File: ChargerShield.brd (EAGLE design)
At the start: 123.2 x 53.3 mm, 42 parts, among them IC1 LM324N, Q1 BD648, Q2 BC140-10, Q3 BC548, T2 BC548, X1 +5V, X2 Battery, X3 VCC

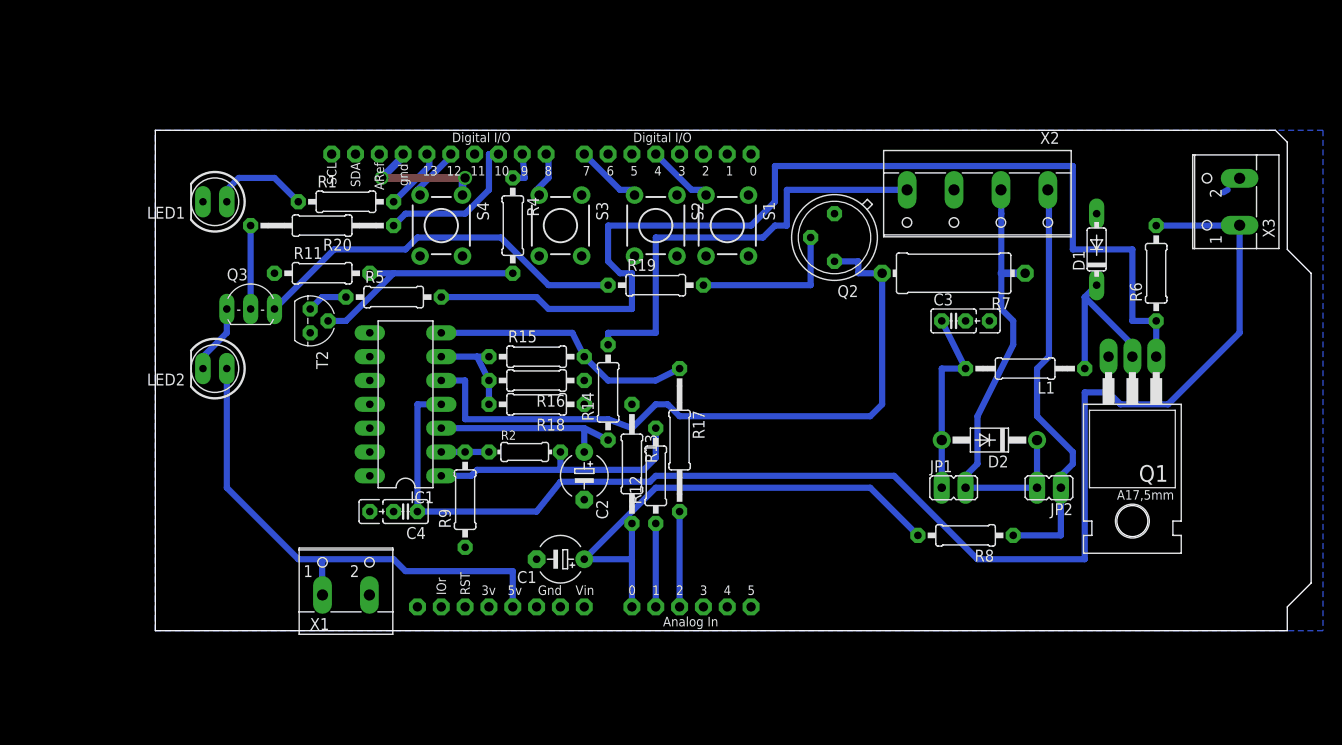
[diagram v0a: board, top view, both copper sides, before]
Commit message: changes to reflect current breadboard layout
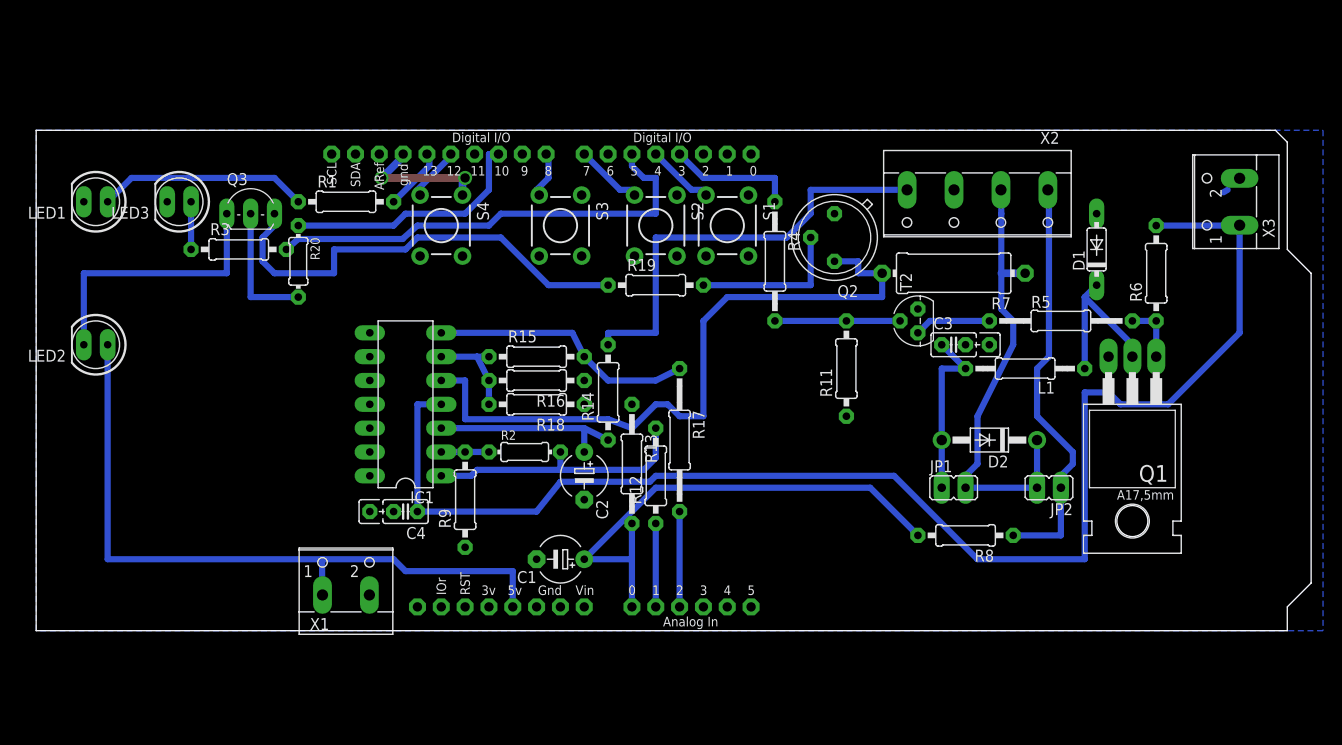
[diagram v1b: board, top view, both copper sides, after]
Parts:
- added LED3: CHRG2, bigger:LED5MM_BIG
- added R3: (no value), rcl:0207/10
- LED1: value (none) -> CHRG1
- R20: device rcl:0207/15 -> rcl:0204/7
- R4: device rcl:0207/10 -> rcl:0207/12
- R5: device rcl:0207/10 -> rcl:0207/15
- moved R5 71.2 mm to (96.5, 33.0)
- moved T2 64.8 mm to (81.3, 33.0), turned to 90 degrees
- moved R11 56.8 mm to (73.7, 27.9), turned to 90 degrees
- moved R4 28.2 mm to (66.0, 39.4)
- moved LED2 13.0 mm to (-6.35, 30.5)
- moved LED1 12.7 mm to (-6.35, 45.7)
- moved Q3 10.2 mm to (10.2, 45.7)
- moved R20 4.58 mm to (15.2, 39.4), turned to 270 degrees
- moved C3 2.54 mm to (85.1, 30.5)
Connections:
- net N$24 renamed PWM_DISCHARGE1
- removed net PWM: R4.1, U$1.D9
- new net I_BATT2: U$1.A4
- new net I_DISC2: U$1.A5
- new net N$19: R3.2, U$1.D5
- new net N$24: LED3.A, R3.1
- new net PWM_CHARGE1: R4.1, U$1.D3
- new net PWM_CHARGE2: U$1.D9
- new net PWM_DISCHARGE2: U$1.D11
- new net U_BATT2: U$1.A3
- net GND: now also LED3.K
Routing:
- net N$7: track 115.1 -> 6.35 mm
- net N$19: track 0.00 -> 49.0 mm
- net N$21: track 7.40 -> 29.2 mm
- net +5V: track 54.5 -> 74.2 mm
- net PWM_CHARGE1: track 0.00 -> 13.8 mm
- net N$2: track 10.5 -> 22.4 mm
- net N$5: track 24.3 -> 13.3 mm
- net PWM_DISCHARGE1: track 16.8 -> 27.0 mm
- net DISC_1: track 40.8 -> 48.1 mm
- net N$20: track 8.89 -> 14.0 mm
- net N$24: track 0.00 -> 5.08 mm
- net PWM: track 4.08 -> 0.00 mm
- net N$6: track 4.34 -> 8.15 mm
- net N$10: track 20.9 -> 18.8 mm
- net I_SENSE: track 47.6 -> 46.9 mm
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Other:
- board size 123.2 x 53.3 mm -> 135.9 x 53.3 mm

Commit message: reference voltage
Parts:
- removed Q3: BC548, transistor-npn:TO92-EBC
- added C5: 3µ3, rcl:E5-5
- added IC2: TL431, AWJLEagleLib:TO92
- added LED4: (no value), bigger:LED5MM_BIG
- added R21: 200, rcl:0204/7
- added R22: 4k7, rcl:0207/10
- added R23: 470, rcl:0204/7
- added R24: 1k, rcl:0207/10
- Q2: value BC140-10 -> BUZ11; device transistor-npn:TO39 -> transistor-fet:TO220
- R1, R3: value (none) -> 470
- R12: device rcl:0207/10 -> rcl:0207/12
- R13, R4: device rcl:0207/12 -> rcl:0207/10
- R19: value 200 -> 1k
- R20: value 1k -> 470; device rcl:0204/7 -> rcl:0207/10
- R9: device rcl:0207/10 -> rcl:0204/7
- moved R7 31.4 mm to (63.5, 15.2), turned to 270 degrees
- moved Q2 25.4 mm to (71.1, 16.5)
- moved R1 17.3 mm to (3.81, 50.8)
- moved R19 16.1 mm to (38.1, 41.9), turned to 270 degrees
- moved R11 11.7 mm to (76.2, 39.4), turned to 270 degrees
- moved R2 8.54 mm to (33.7, 12.7), turned to 270 degrees
- moved R12 8.13 mm to (47.0, 11.4), turned to 180 degrees
- moved R20 6.48 mm to (8.89, 38.1), turned to 180 degrees
- moved C3 6.35 mm to (81.3, 25.4), turned to 180 degrees
- moved R4 5.08 mm to (71.1, 39.4)
- moved L1 2.84 mm to (91.4, 25.4)
- moved R9 2.84 mm to (35.6, 12.7)
- moved R8 2.54 mm to (83.8, 10.2)
- moved C1 1.27 mm to (43.2, 6.35)
- moved R13 1.27 mm to (50.8, 19.1)
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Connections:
- removed net DISC_1: Q3.E, R19.1
- removed net N$12: IC1.5, Q2.3, R7.2
- new net N$25: Q2.3, R24.2, R7.1
- new net N$27: IC2.1, IC2.3, R21.1, R22.2
- new net N$28: R22.1, U$1.AREF
- new net N$29: C5.+, IC1.5, R24.1
- net +5V: now also C4.1, IC1.4, R21.2; no longer LED2.A
- net GND: now also C5.-, IC2.2, LED2.K, LED4.K, R7.2; no longer Q2.1
- net N$13: now also Q2.2; no longer R7.1
- net N$18: now also Q2.1; no longer Q2.2
- net N$20: now also LED2.A; no longer Q3.B
- net N$21: now also LED4.A, R23.2; no longer LED2.K, Q3.C
- net PWM_DISCHARGE1: now also R19.1
- net PWM_DISCHARGE2: now also R23.1
- net VCC: no longer C4.1, IC1.4
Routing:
- net VCC: track 152.7 -> 44.5 mm
- net N$12: track 73.0 -> 0.00 mm
- net DISC_1: track 48.1 -> 0.00 mm
- net N$13: track 48.9 -> 95.9 mm
- net N$18: track 16.5 -> 48.8 mm, vias 0 -> 2
- net N$25: track 0.00 -> 24.2 mm
- net N$1: track 6.91 -> 29.4 mm
- net N$27: track 0.00 -> 16.5 mm
- net PWM_DISCHARGE1: track 27.0 -> 43.3 mm
- net N$29: track 0.00 -> 14.8 mm
- net N$2: track 22.4 -> 8.89 mm
- net N$21: track 29.2 -> 42.2 mm
- net N$11: track 28.7 -> 18.4 mm
- net +5V: track 74.2 -> 81.8 mm
- net PWM_CHARGE1: track 13.8 -> 20.1 mm
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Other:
- board size 135.9 x 53.3 mm -> 135.9 x 55.9 mm

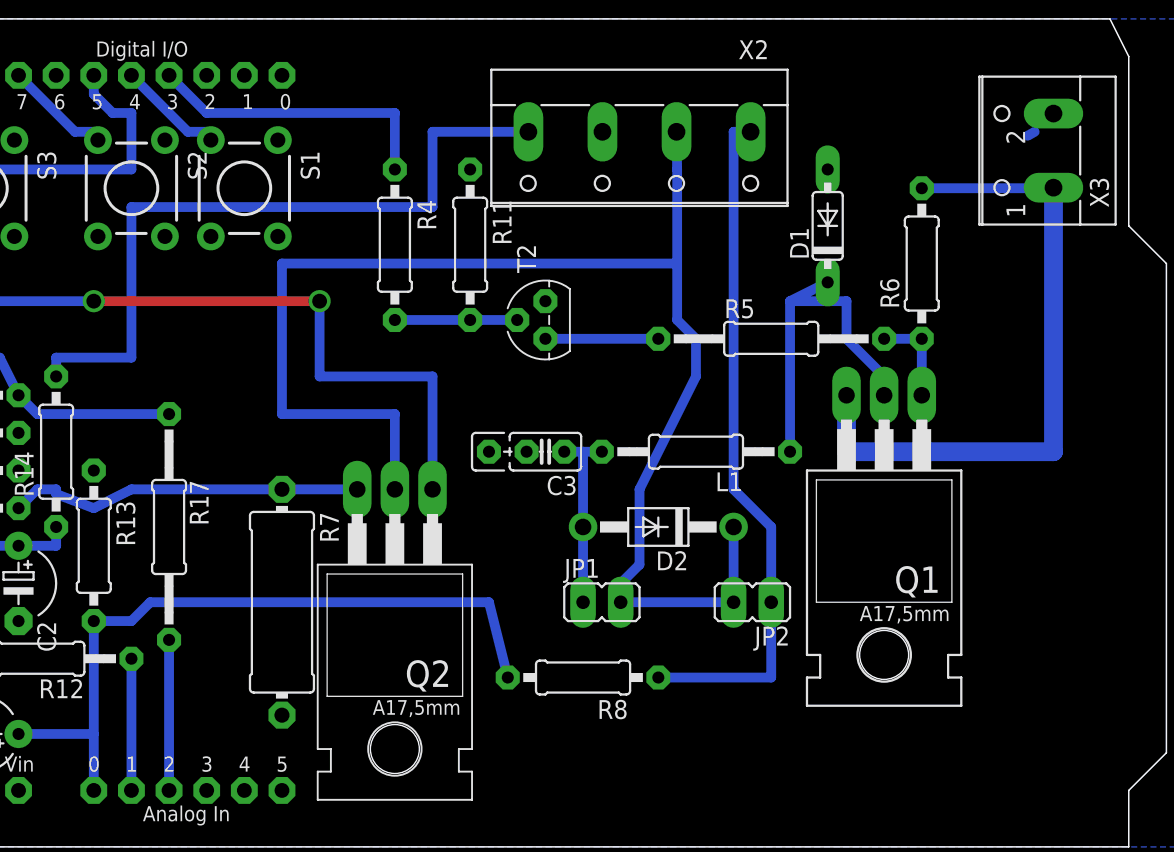
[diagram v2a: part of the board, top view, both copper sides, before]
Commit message: bigger power traces
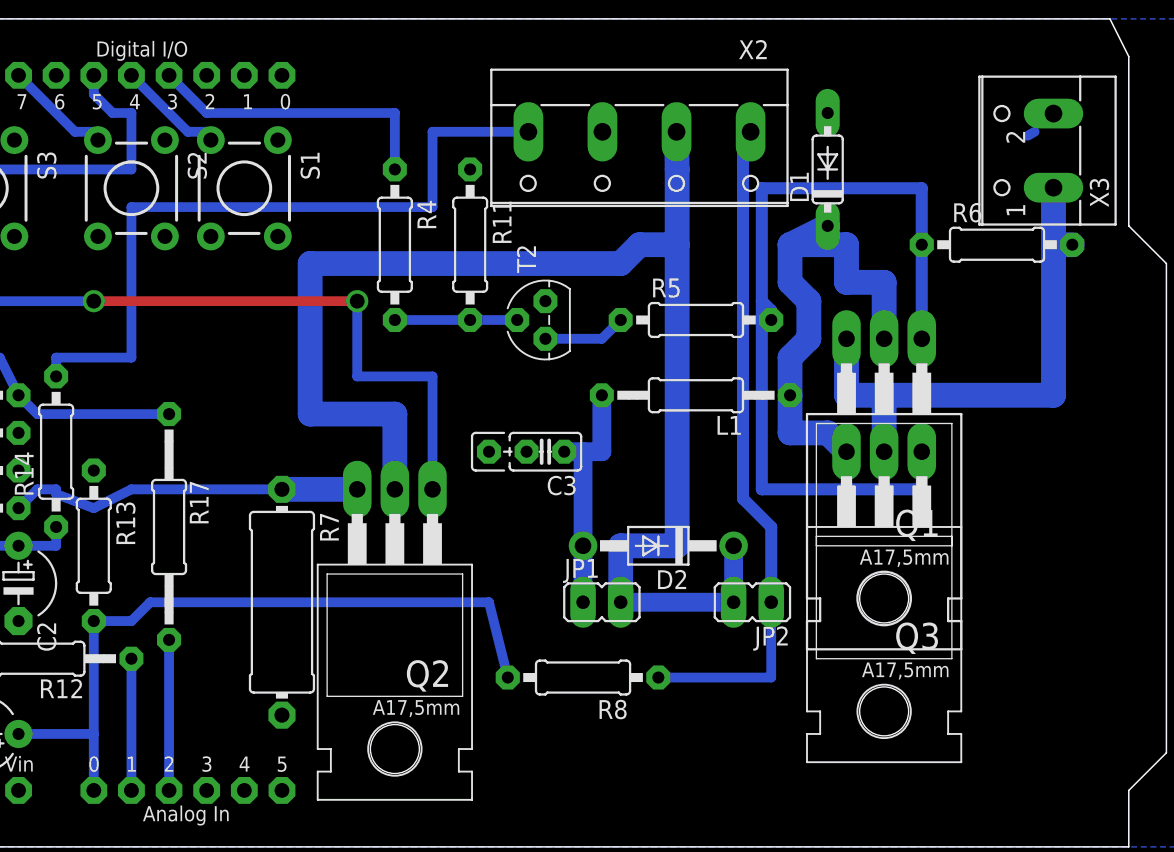
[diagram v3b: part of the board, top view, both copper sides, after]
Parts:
- added Q3: BUZ171, transistor-fet:TO220
- R5: device rcl:0207/15 -> rcl:0207/10
- moved R5 5.24 mm to (91.4, 34.3)
- moved R6 5.24 mm to (111.8, 39.4), turned to 0 degrees
- moved D1 3.81 mm to (100.3, 44.5)
- moved L1 3.81 mm to (91.4, 29.2)
- moved Q1 3.81 mm to (104.1, 26.7)
- moved D2 1.27 mm to (88.9, 19.1)
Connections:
- net N$7: now also Q3.1
- net N$9: now also Q3.3
- net VCC: now also Q3.2
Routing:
- net N$7: track 6.35 -> 56.1 mm
- net N$9: track 25.5 -> 34.9 mm
- net VCC: track 44.5 -> 36.9 mm
- net N$10: track 12.7 -> 16.5 mm
- net N$13: track 95.9 -> 93.2 mm
- net N$6: track 7.62 -> 5.61 mm
- net N$8: track 46.8 -> 45.5 mm

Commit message: bigger board
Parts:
- added JP3: (no value), bigger:JP2
- added R25: 4k7, rcl:0204/7
- added U$2: DS1820TO92, Ava:DS1820
- R19: device rcl:0207/10 -> rcl:0204/7
- moved X2 11.4 mm to (87.6, 57.1)
- moved R19 3.18 mm to (35.6, 43.8)
- moved R23 2.54 mm to (38.1, 44.5)
- moved IC2 1.27 mm to (31.8, 35.6)
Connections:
- new net N$12: JP3.2, R25.1, U$1.D2, U$2.DQ
- net +5V: now also R25.2
- net GND: now also JP3.1, JP3.3, U$2.GND, U$2.VDD
- net PWM_CHARGE2: now also U$1.D11; no longer U$1.D9
- net PWM_DISCHARGE2: now also U$1.D9; no longer U$1.D11
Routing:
- net +5V: track 81.8 -> 193.4 mm
- net N$12: track 0.00 -> 19.2 mm
- net N$8: track 45.5 -> 57.0 mm
- net N$13: track 93.2 -> 104.7 mm
- net I_SENSE: track 48.4 -> 55.0 mm
- net N$18: track 48.8 -> 53.0 mm
- net PWM_DISCHARGE1: track 43.3 -> 40.8 mm
- net N$21: track 42.2 -> 44.8 mm
- net PWM_CHARGE1: track 20.1 -> 17.9 mm
- net N$27: track 16.5 -> 15.2 mm
- net PWM_DISCHARGE2: track 3.32 -> 4.06 mm
- net N$17: track 27.5 -> 28.1 mm
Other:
- board size 135.9 x 55.9 mm -> 135.9 x 73.7 mm
